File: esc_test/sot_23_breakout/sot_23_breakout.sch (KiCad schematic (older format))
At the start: 3 parts, among them P1 CONN_01X02, P2 CONN_01X02, Q1 Q_NMOS_GDS

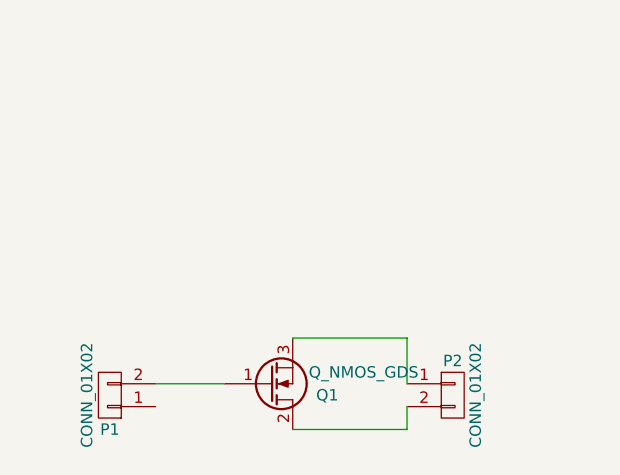
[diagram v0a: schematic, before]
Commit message: Final test breakout boards sent to Oshpark.
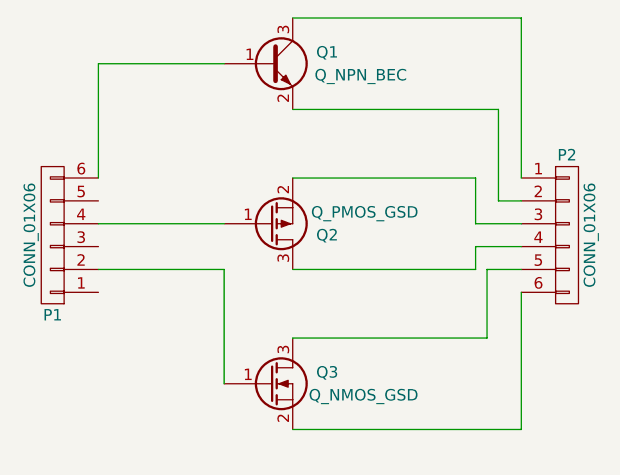
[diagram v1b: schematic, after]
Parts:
- removed P1, P2: CONN_01X02, Pin_Headers:Pin_Header_Straight_1x02, symbol CONN_01X02
- removed Q1: Q_NMOS_GDS, Housings_SOT-23_SOT-143_TSOT-6:SOT-23, symbol Q_NMOS_GDS
- added P1, P2: CONN_01X06, Pin_Headers:Pin_Header_Straight_1x06, symbol CONN_01X06
- added Q1: Q_NPN_BEC, Housings_SOT-23_SOT-143_TSOT-6:SOT-23, symbol Q_NPN_BEC
- added Q2: Q_PMOS_GSD, Housings_SOT-23_SOT-143_TSOT-6:SOT-23, symbol Q_PMOS_GSD
- added Q3: Q_NMOS_GSD, Housings_SOT-23_SOT-143_TSOT-6:SOT-23, symbol Q_NMOS_GSD
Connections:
- new net: P1.2 (P2), Q3.1 (G)
- new net: P2.6 (P6), Q3.2 (S)
- new net: P2.5 (P5), Q3.3 (D)
- new net: P1.4 (P4), Q2.1 (G)
- new net: P2.3 (P3), Q2.2 (S)
- new net: P2.4 (P4), Q2.3 (D)
- new net: P1.6 (P6), Q1.1 (B)
- new net: P2.2 (P2), Q1.2 (E)
- new net: P2.1 (P1), Q1.3 (C)
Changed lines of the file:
@@
 LIBS:contrib
 LIBS:valves
+LIBS:sot_23_breakout-cache
 EELAYER 25 0
 EELAYER END
@@
 $EndDescr
 $Comp
-L CONN_01X02 P1
-U 1 1 558B4DEF
-P 4900 3700
-F 0 "P1" H 4900 3850 50  0000 C CNN
-F 1 "CONN_01X02" V 5000 3700 50  0000 C CNN
-F 2 "Pin_Headers:Pin_Header_Straight_1x02" H 4900 3700 60  0001 C CNN
-F 3 "" H 4900 3700 60  0000 C CNN
-	1    4900 3700
-	-1   0    0    1
-$EndComp
-$Comp
-L CONN_01X02 P2
-U 1 1 558B4E1C
-P 6400 3700
-F 0 "P2" H 6400 3850 50  0000 C CNN
-F 1 "CONN_01X02" V 6500 3700 50  0000 C CNN
-F 2 "Pin_Headers:Pin_Header_Straight_1x02" H 6400 3700 60  0001 C CNN
-F 3 "" H 6400 3700 60  0000 C CNN
-	1    6400 3700
+L Q_NMOS_GSD Q3
+U 1 1 558F876E
+P 5600 3650
+F 0 "Q3" H 5900 3700 50  0000 R CNN
+F 1 "Q_NMOS_GSD" H 6250 3600 50  0000 R CNN
+F 2 "Housings_SOT-23_SOT-143_TSOT-6:SOT-23" H 5800 3750 29  0001 C CNN
+F 3 "" H 5600 3650 60  0000 C CNN
+	1    5600 3650
 	1    0    0    -1
 $EndComp
 $Comp
-L Q_NMOS_GDS Q1
-U 1 1 558B4E99
-P 5600 3650
-F 0 "Q1" H 5900 3700 50  0000 R CNN
-F 1 "Q_NMOS_GDS" H 6250 3600 50  0000 R CNN
-F 2 "Housings_SOT-23_SOT-143_TSOT-6:SOT-23" H 5800 3750 29  0001 C CNN
-F 3 "" H 5600 3650 60  0000 C CNN
-	1    5600 3650
+L Q_PMOS_GSD Q2
+U 1 1 558F87A1
+P 5600 2950
+F 0 "Q2" H 5900 3000 50  0000 R CNN
+F 1 "Q_PMOS_GSD" H 6250 2900 50  0000 R CNN
+F 2 "Housings_SOT-23_SOT-143_TSOT-6:SOT-23" H 5800 3050 29  0001 C CNN
+F 3 "" H 5600 2950 60  0000 C CNN
+	1    5600 2950
 	1    0    0    1
 $EndComp
+$Comp
+L Q_NPN_BEC Q1
+U 1 1 558F87DC
+P 5600 2250
+F 0 "Q1" H 5900 2300 50  0000 R CNN
+F 1 "Q_NPN_BEC" H 6200 2200 50  0000 R CNN
+F 2 "Housings_SOT-23_SOT-143_TSOT-6:SOT-23" H 5800 2350 29  0001 C CNN
+F 3 "" H 5600 2250 60  0000 C CNN
+	1    5600 2250
+	1    0    0    -1
+$EndComp
+$Comp
+L CONN_01X06 P2
+U 1 1 558F881E
+P 6900 3000
+F 0 "P2" H 6900 3350 50  0000 C CNN
+F 1 "CONN_01X06" V 7000 3000 50  0000 C CNN
+F 2 "Pin_Headers:Pin_Header_Straight_1x06" H 6900 3000 60  0001 C CNN
+F 3 "" H 6900 3000 60  0000 C CNN
+	1    6900 3000
+	1    0    0    -1
+$EndComp
+$Comp
+L CONN_01X06 P1
+U 1 1 558F8843
+P 4650 3000
+F 0 "P1" H 4650 3350 50  0000 C CNN
+F 1 "CONN_01X06" V 4750 3000 50  0000 C CNN
+F 2 "Pin_Headers:Pin_Header_Straight_1x06" H 4650 3000 60  0001 C CNN
+F 3 "" H 4650 3000 60  0000 C CNN
+	1    4650 3000
+	-1   0    0    1
+$EndComp
 Wire Wire Line
-	5700 3850 6200 3850
+	5700 2050 6700 2050
 Wire Wire Line
-	6200 3850 6200 3750
+	6700 2050 6700 2750
 Wire Wire Line
-	5700 3450 6200 3450
+	5700 2450 6600 2450
 Wire Wire Line
-	6200 3450 6200 3650
+	6600 2450 6600 2850
 Wire Wire Line
-	5400 3650 5100 3650
+	6600 2850 6700 2850
+Wire Wire Line
+	5700 2750 6500 2750
+Wire Wire Line
+	6500 2750 6500 2950
+Wire Wire Line
+	6500 2950 6700 2950
+Wire Wire Line
+	5700 3150 6500 3150
+Wire Wire Line
+	6500 3150 6500 3050
+Wire Wire Line
+	6500 3050 6700 3050
+Wire Wire Line
+	5700 3450 6550 3450
+Wire Wire Line
+	6550 3450 6550 3150
+Wire Wire Line
+	6550 3150 6700 3150
+Wire Wire Line
+	5700 3850 6700 3850
+Wire Wire Line
+	6700 3850 6700 3250
+Wire Wire Line
+	4850 2750 4850 2250
+Wire Wire Line
+	4850 2250 5400 2250
+Wire Wire Line
+	4850 2950 5400 2950
+Wire Wire Line
+	5400 3650 5400 3150
+Wire Wire Line
+	5400 3150 4850 3150
 $EndSCHEMATC
